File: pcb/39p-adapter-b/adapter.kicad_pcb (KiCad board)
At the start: 2 copper layers, 26.6 x 17.9 mm, 2 parts, among them J1 FH12-40S-0.5SH, J3 10064555-392120HLF

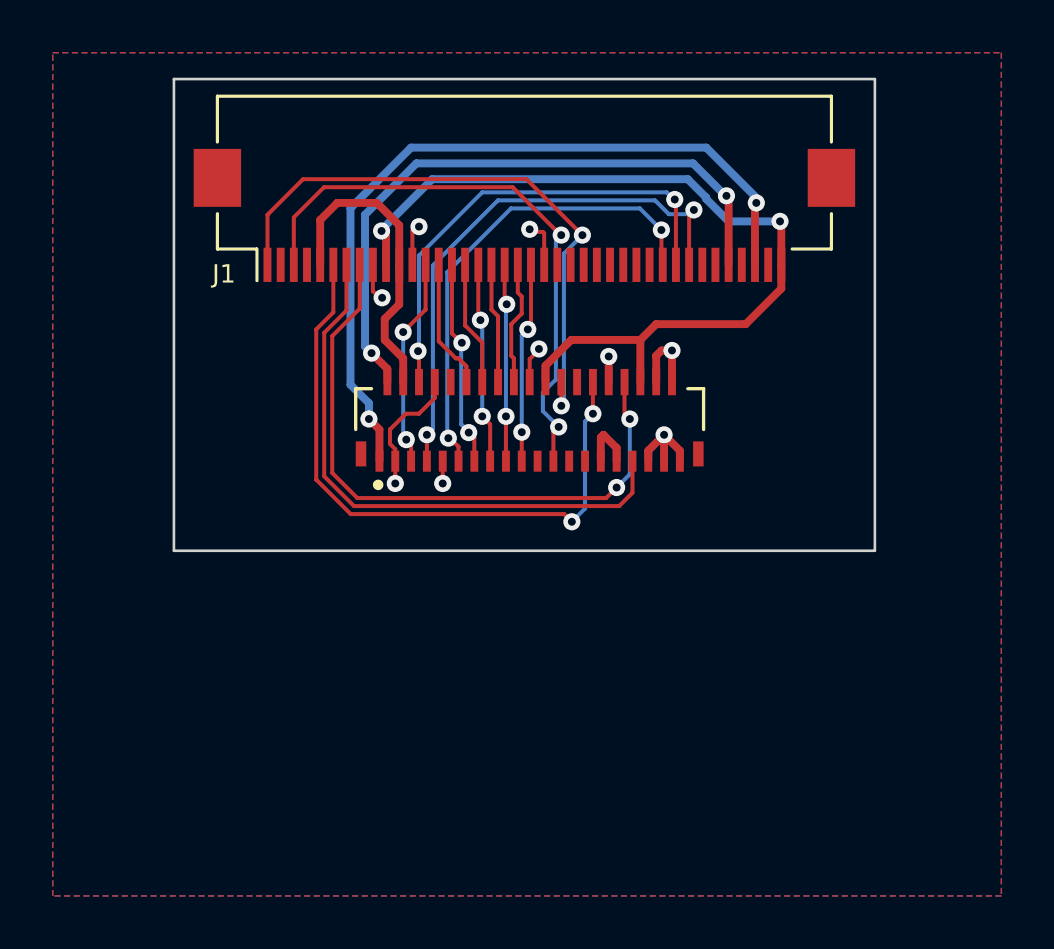
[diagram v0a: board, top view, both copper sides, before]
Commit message: Update 39p-b adapter design
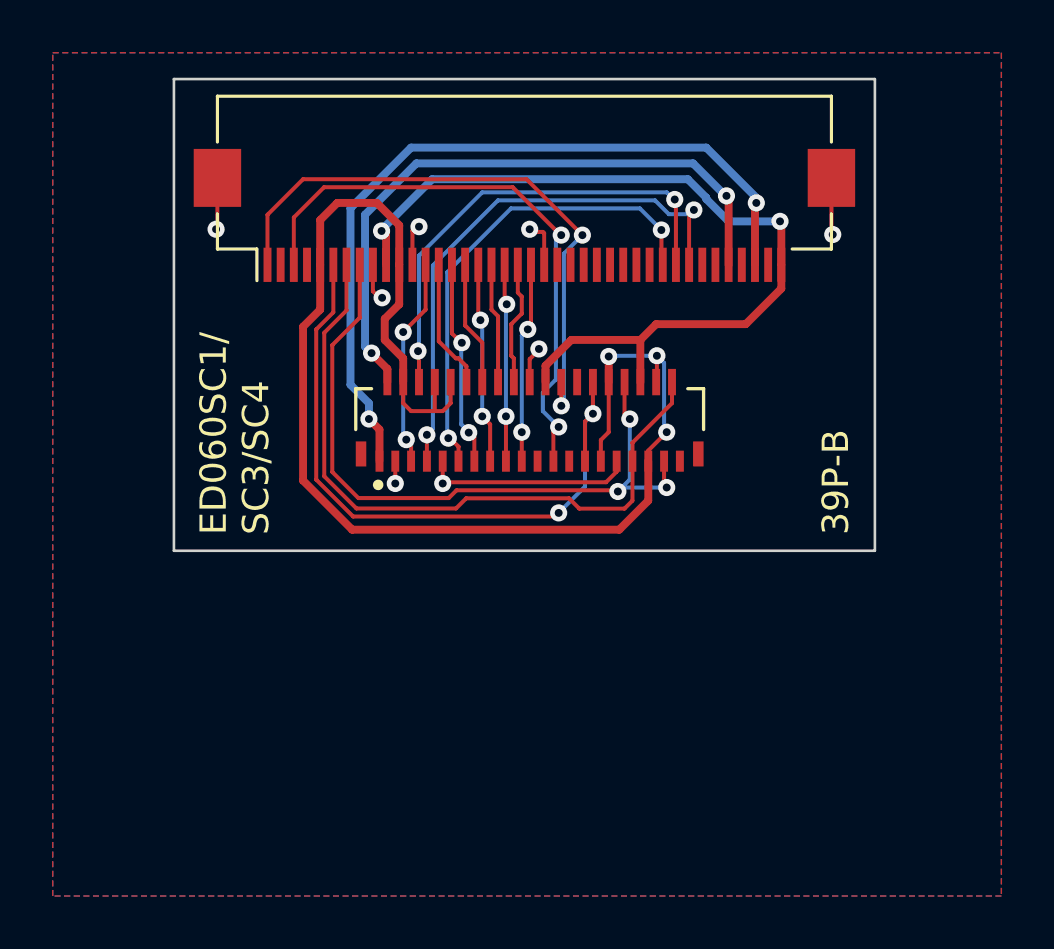
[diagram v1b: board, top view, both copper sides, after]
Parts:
- J3: value 10064555-392120HLF -> FH26W-39S-0.3SHW(60)
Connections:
- J3 pad 10: unconnected-(J3-Pad10) -> +3V3
- J3 pad 20: GND -> unconnected-(J3-Pin_20-Pad20)
- J3 pad 27: unconnected-(J3-Pad27) -> /GDOE
- J3 pad 29: GND -> +3V3
- J3 pad 30: GND -> +3V3
- J3 pad 35: GND -> +3V3
- J3 pad 36: GND -> +3V3
- J3 pad 37: GND -> /GDSP
- J3 pad 38: GND -> /GDCLK
- J3 pad 39: GND -> unconnected-(J3-Pin_39-Pad39)
- J3 pad 8: GND -> +3V3
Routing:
- net +3V3: track 11.8 -> 52.3 mm, vias 0 -> 3
- net /GDCLK: track 21.9 -> 26.1 mm
- net GND: track 21.9 -> 18.1 mm, vias 9 -> 7
- net /GDSP: track 24.0 -> 27.2 mm, vias 2 -> 3
- net unconnected-(J3-Pin_20-Pad20): track 0.00 -> 1.40 mm, vias 0 -> 1
- net /GDOE: track 24.4 -> 25.7 mm
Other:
- board text added: "39P-B"
- board text added: "ED060SC1/ SC3/SC4"
